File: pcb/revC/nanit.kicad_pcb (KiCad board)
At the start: 2 copper layers, 31.2 x 53.3 mm, 74 parts, among them J1 USB_B_Micro, J2 AVR-ISP-6, P1 SSD1306 OLED 128x64 0.96", Q1 BC857, Q2 IRLML6344, Q4 BC847, SW1 Button 1, SW2 Button 2, U1 LTC4054ES5-4.2, U2 ATmega328P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

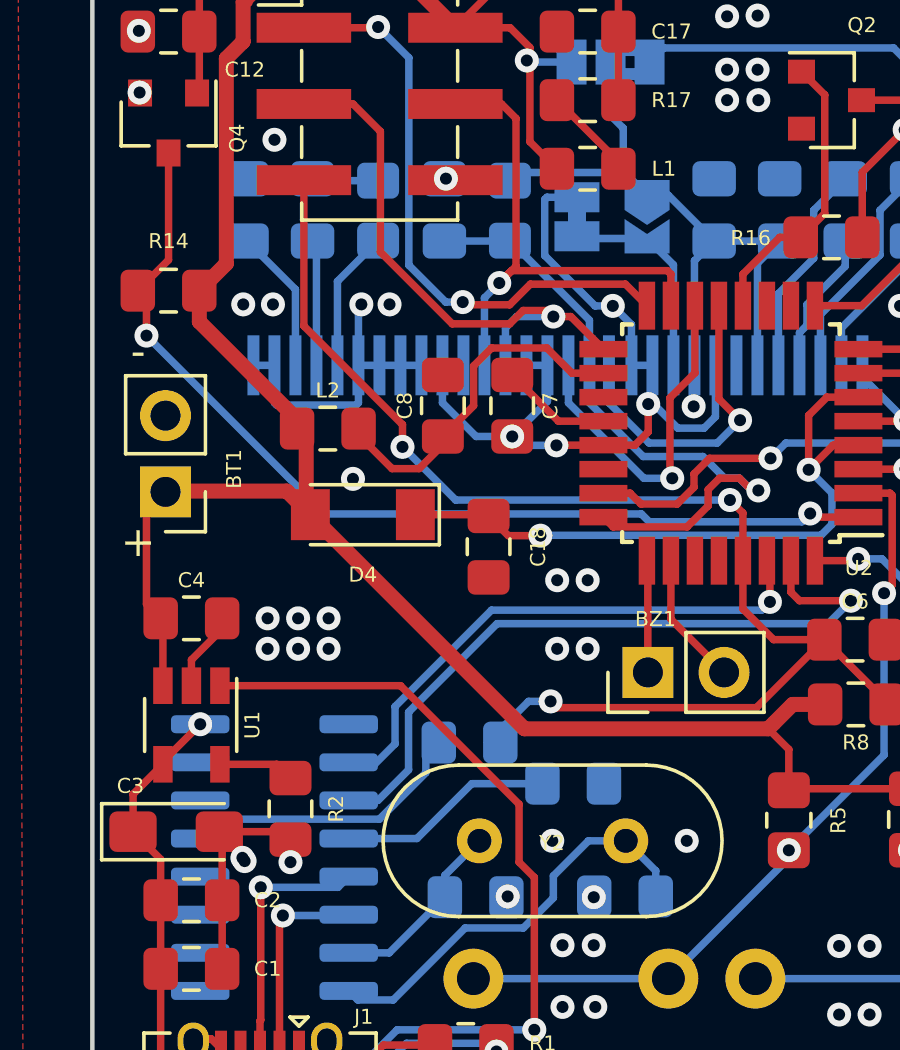
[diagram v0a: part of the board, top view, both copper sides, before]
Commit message: PCB rev.C (OLED version)
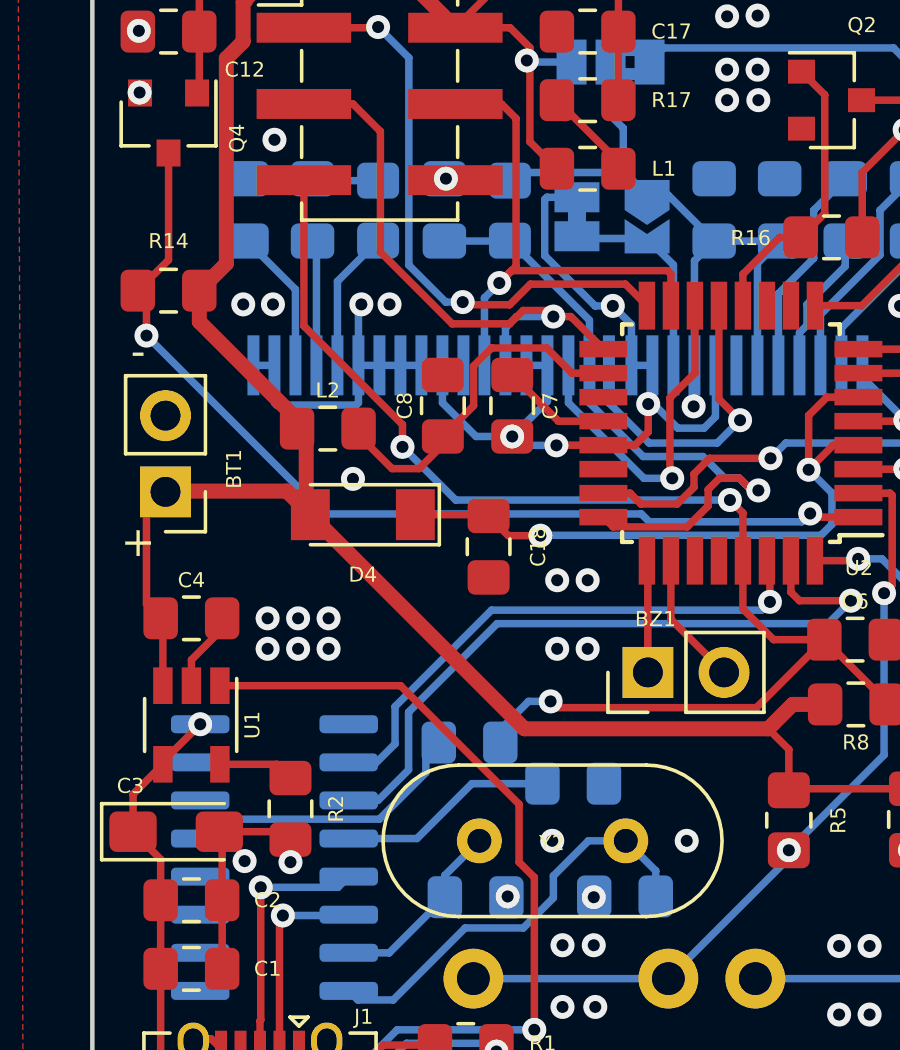
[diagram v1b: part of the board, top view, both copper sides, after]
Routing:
- net GNDD: vias 69 -> 68
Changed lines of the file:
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@@
       (primitives
         (gr_poly (pts
-          (xy -0.5 0.75)
-          (xy 0.5 0.75)
-          (xy 1 0)
-          (xy 0.5 -0.75)
-          (xy -0.5 -0.75)
-        ) (width 0) (fill yes))
+            (xy 1 0)
+            (xy 0.5 0.75)
+            (xy -0.5 0.75)
+            (xy -0.5 -0.75)
+            (xy 0.5 -0.75)
+          ) (width 0) (fill yes))
       ))
     (pad "2" smd custom locked (at 0.725 0 270) (size 0.3 0.3) (layers "B.Cu" "B.Mask")
@@
       (primitives
         (gr_poly (pts
-          (xy -0.65 0.75)
-          (xy 0.5 0.75)
-          (xy 0.5 -0.75)
-          (xy -0.65 -0.75)
-          (xy -0.15 0)
-        ) (width 0) (fill yes))
+            (xy 0.5 0.75)
+            (xy -0.65 0.75)
+            (xy -0.15 0)
+            (xy -0.65 -0.75)
+            (xy 0.5 -0.75)
+          ) (width 0) (fill yes))
       ))
   )
@@
       (effects (font (size 1 1) (thickness 0.15)) (justify mirror))
     )
-    (fp_poly (pts (xy -0.25 0.3)
-      (xy 0.25 0.3)
-      (xy 0.25 -0.3)
-      (xy -0.25 -0.3)) (layer "B.Cu") (width 0) (fill solid))
+    (fp_poly (pts
+        (xy -0.25 0.3)
+        (xy 0.25 0.3)
+        (xy 0.25 -0.3)
+        (xy -0.25 -0.3)
+      ) (layer "B.Cu") (width 0) (fill solid))
     (fp_line (start -1.4 -1) (end -1.4 1) (layer "B.SilkS") (width 0.12))
     (fp_line (start 1.4 -1) (end -1.4 -1) (layer "B.SilkS") (width 0.12))
@@
       (effects (font (size 1 1) (thickness 0.15)) (justify mirror))
     )
-    (fp_poly (pts (xy -0.9 0.6)
-      (xy -0.4 0.6)
-      (xy -0.4 0.2)
-      (xy -0.9 0.2)) (layer "B.Cu") (width 0) (fill solid))
-    (fp_poly (pts (xy -0.9 -0.2)
-      (xy -0.4 -0.2)
-      (xy -0.4 -0.6)
-      (xy -0.9 -0.6)) (layer "B.Cu") (width 0) (fill solid))
+    (fp_poly (pts
+        (xy -0.9 0.6)
+        (xy -0.4 0.6)
+        (xy -0.4 0.2)
+        (xy -0.9 0.2)
+      ) (layer "B.Cu") (width 0) (fill solid))
+    (fp_poly (pts
+        (xy -0.9 -0.2)
+        (xy -0.4 -0.2)
+        (xy -0.4 -0.6)
+        (xy -0.9 -0.6)
+      ) (layer "B.Cu") (width 0) (fill solid))
     (fp_line (start -2.05 1) (end 2.05 1) (layer "B.SilkS") (width 0.12))
     (fp_line (start 2.05 1) (end 2.05 -1) (layer "B.SilkS") (width 0.12))
@@
   (via (at 122.174 110.998) (size 0.8) (drill 0.4) (layers "F.Cu" "B.Cu") (net 10))
   (via (at 129.63 118.4148) (size 0.8) (drill 0.4) (layers "F.Cu" "B.Cu") (net 10))
-  (via (at 119.301473 118.981771) (size 0.8) (drill 0.4) (layers "F.Cu" "B.Cu") (net 10))
   (via (at 131.064 123.952) (size 0.8) (drill 0.4) (layers "F.Cu" "B.Cu") (net 10))
   (via (at 129.794 109.728) (size 0.8) (drill 0.4) (layers "F.Cu" "B.Cu") (net 10))

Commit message: revD
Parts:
- removed R5: 10k, Resistor_SMD:R_0805_2012Metric_Pad1.20x1.40mm_HandSolder
- J1: footprint Connector_USB:USB_Micro-AB_Molex_47590-0001 -> Connector_USB:USB_Micro-B_Amphenol_10118194_Horizontal
- R4*1: renamed from R4; value 910k -> 390..910k
- moved J1 1.35 mm to (119.9, 126.7)
- renumbered C24 to C24*1, R3 to R3*1
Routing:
- net GNDD: track 73.0 -> 62.6 mm, vias 68 -> 74
- net VCC: track 86.0 -> 85.1 mm
- net Net-(J1-Pad3): track 8.47 -> 7.67 mm
- net Net-(C1-Pad1): track 24.4 -> 25.1 mm, vias 1 -> 3
- net Net-(J1-Pad2): track 6.69 -> 7.23 mm
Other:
- outline, holes or cut-outs redrawn
